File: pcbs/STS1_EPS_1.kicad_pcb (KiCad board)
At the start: 4 copper layers, 81 x 85 mm, 57 parts, among them J2 Panel X+, J3 Battery Pack, J4 Panel X-, J5 Panel Y+, J6 Panel Y-, J7 Panel Z+, Q1 SI7135DP-T1-GE3, U1 LTC4020EUHFPBF, U10 MAX11632EEGT, U4 BQ29209DRBT, U5 MAX11632EEGT, U6 MAX11632EEGT, U7 MAX11632EEGT, U8 MAX11632EEGT, U9 MAX11632EEGT

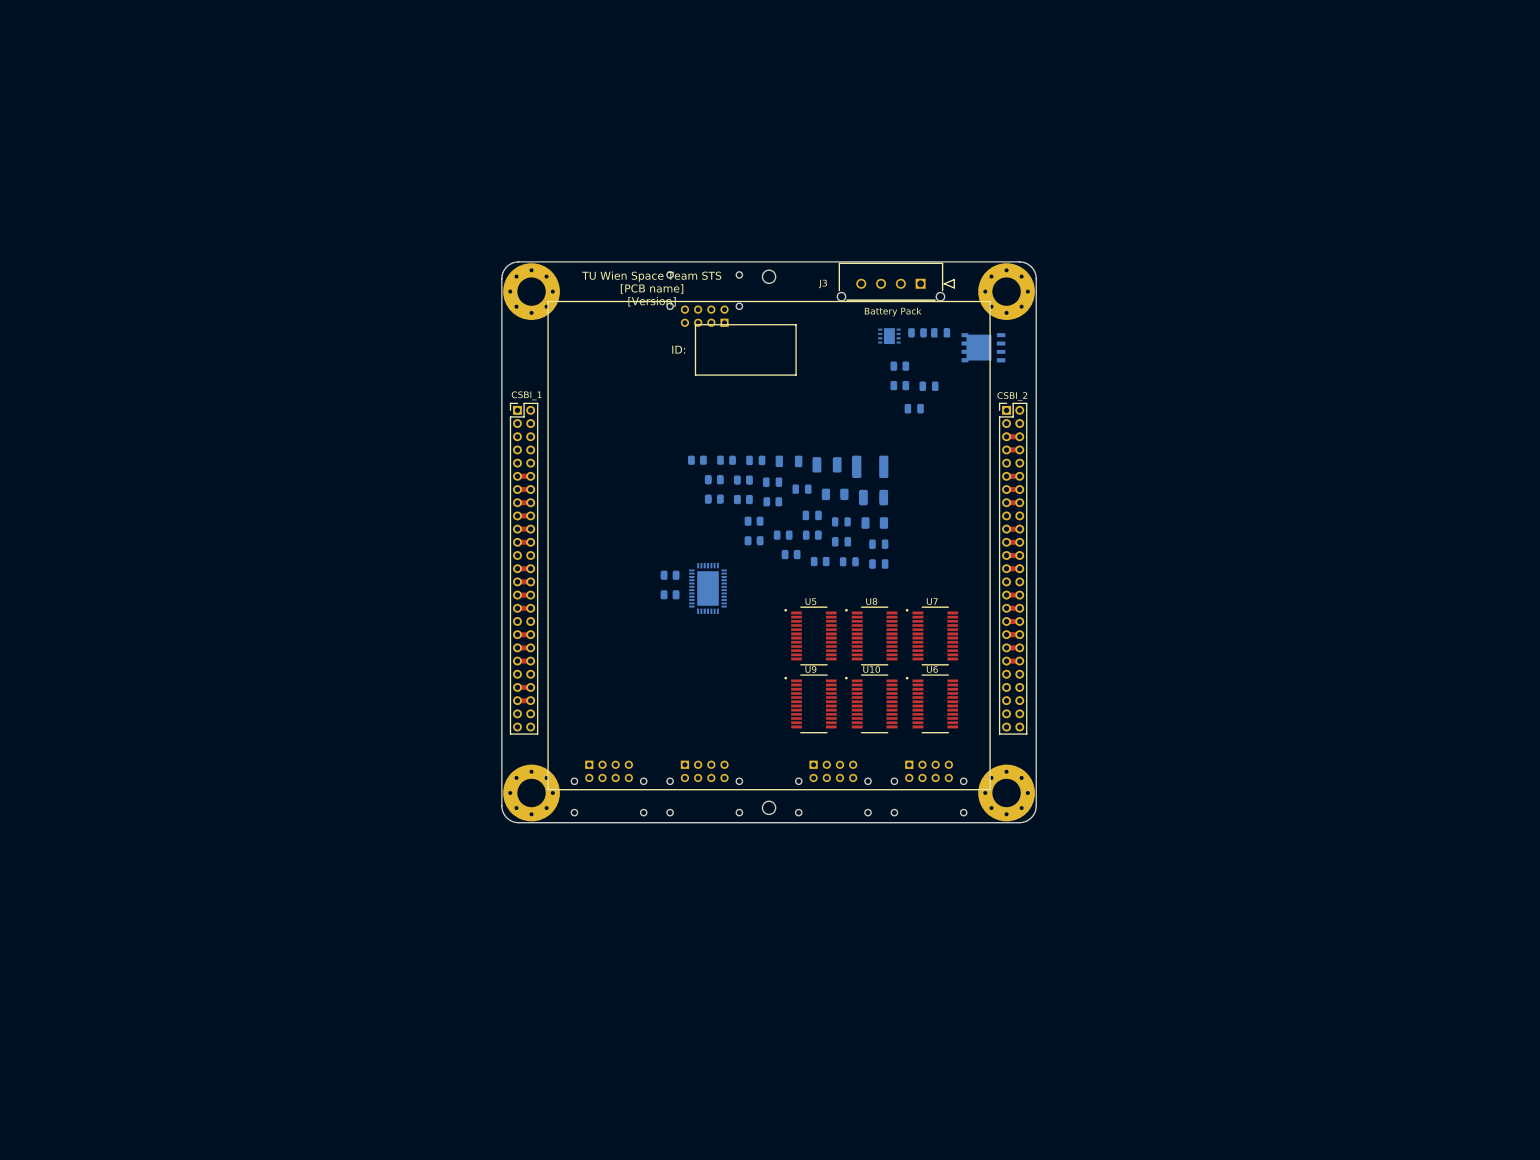
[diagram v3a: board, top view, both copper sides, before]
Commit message: Worked on STS1_EPS_1.
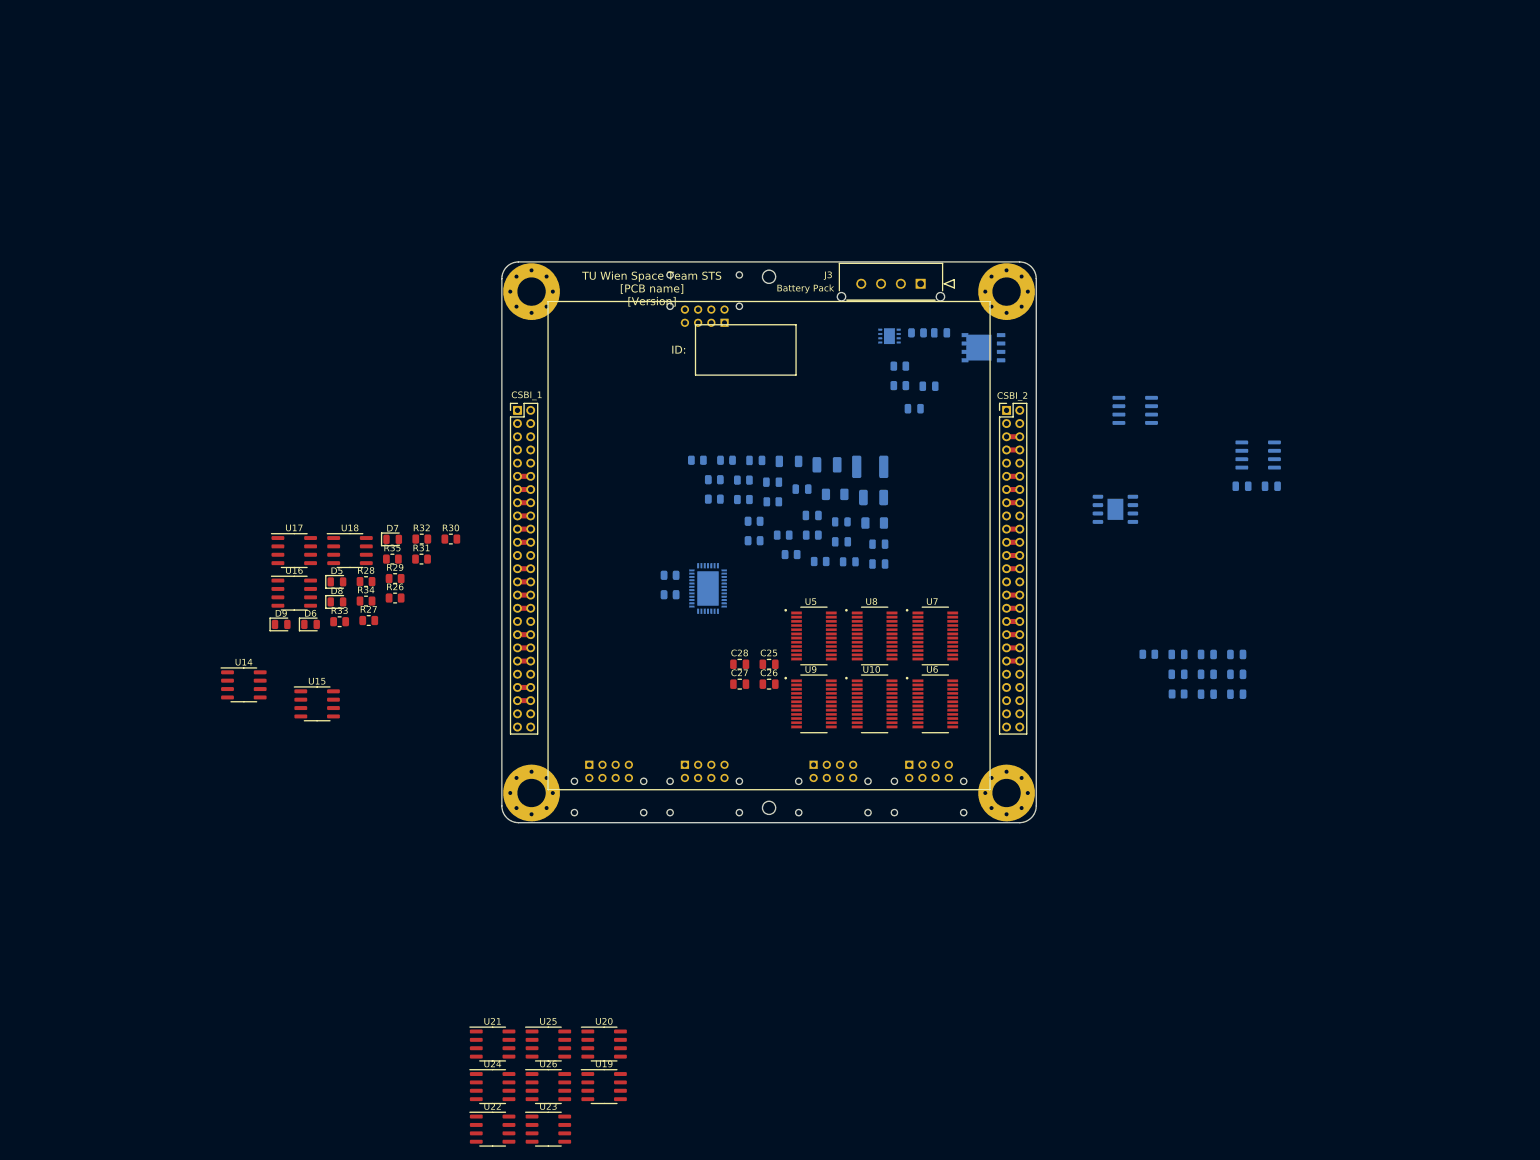
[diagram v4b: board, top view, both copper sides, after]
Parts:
- added C15: 1u, Capacitor_SMD:C_0805_2012Metric, B.Cu at (232.8, 75.8)
- added C16: 1u, Capacitor_SMD:C_0805_2012Metric, B.Cu at (228.3, 75.8)
- added C17: 100n, Capacitor_SMD:C_0805_2012Metric, B.Cu at (218.6, 101.3)
- added C18: 100n, Capacitor_SMD:C_0805_2012Metric, B.Cu at (223.1, 101.3)
- added C19: 100n, Capacitor_SMD:C_0805_2012Metric, B.Cu at (223.1, 104.3)
- added C20: 100n, Capacitor_SMD:C_0805_2012Metric, B.Cu at (227.5, 101.3)
- added C21: 100n, Capacitor_SMD:C_0805_2012Metric, B.Cu at (227.5, 104.3)
- added C22: 100n, Capacitor_SMD:C_0805_2012Metric, B.Cu at (223.1, 107.3)
- added C23: 100n, Capacitor_SMD:C_0805_2012Metric, B.Cu at (218.6, 104.3)
- added C24: 100n, Capacitor_SMD:C_0805_2012Metric, B.Cu at (227.5, 107.3)
- added C25: 100n, Capacitor_SMD:C_0805_2012Metric, F.Cu at (156.6, 102.8)
- added C26: 100n, Capacitor_SMD:C_0805_2012Metric, F.Cu at (156.6, 105.8)
- added C27: 100n, Capacitor_SMD:C_0805_2012Metric, F.Cu at (152.2, 105.8)
- added C28: 100n, Capacitor_SMD:C_0805_2012Metric, F.Cu at (152.2, 102.8)
- added D5: TS4148 RYG, Diode_SMD:D_0805_2012Metric, F.Cu at (91.1, 90.3)
- added D6: TS4148 RYG, Diode_SMD:D_0805_2012Metric, F.Cu at (87.1, 96.8)
- added D7: TS4148 RYG, Diode_SMD:D_0805_2012Metric, F.Cu at (99.6, 83.8)
- added D8: TS4148 RYG, Diode_SMD:D_0805_2012Metric, F.Cu at (91.1, 93.3)
- added D9: TS4148 RYG, Diode_SMD:D_0805_2012Metric, F.Cu at (82.7, 96.8)
- added R24: 87k5, Resistor_SMD:R_0805_2012Metric, B.Cu at (214.2, 101.3)
- added R25: 100k, Resistor_SMD:R_0805_2012Metric, B.Cu at (218.6, 107.3)
- added R26: 332, Resistor_SMD:R_0805_2012Metric, F.Cu at (100.0, 92.7)
- added R27: 3320, Resistor_SMD:R_0805_2012Metric, F.Cu at (96.0, 96.2)
- added R28: 332, Resistor_SMD:R_0805_2012Metric, F.Cu at (95.5, 90.3)
- added R29: 3320, Resistor_SMD:R_0805_2012Metric, F.Cu at (100.0, 89.8)
- added R30: 332, Resistor_SMD:R_0805_2012Metric, F.Cu at (108.4, 83.8)
- added R31: 3320, Resistor_SMD:R_0805_2012Metric, F.Cu at (104.0, 86.8)
- added R32: 332, Resistor_SMD:R_0805_2012Metric, F.Cu at (104.0, 83.8)
- added R33: 3320, Resistor_SMD:R_0805_2012Metric, F.Cu at (91.5, 96.3)
- added R34: 332, Resistor_SMD:R_0805_2012Metric, F.Cu at (95.5, 93.2)
- added R35: 3320, Resistor_SMD:R_0805_2012Metric, F.Cu at (99.5, 86.8)
- added U11: TMCS1101A3B-Q1, Package_SO:SOIC-8_3.9x4.9mm_P1.27mm, B.Cu at (230.8, 71.1)
- added U12: BD50GA5WEFJ, Package_SO:HTSOP-8-1EP_3.9x4.9mm_P1.27mm_EP2.4x3.2mm, B.Cu at (209.1, 79.3)
- added U13: TMCS1101A3B-Q1, Package_SO:SOIC-8_3.9x4.9mm_P1.27mm, B.Cu at (212.1, 64.3)
- added U14: LM334M, Package_SO:SOIC-8_3.9x4.9mm_P1.27mm, F.Cu at (77.0, 105.9)
- added U15: LM334M, Package_SO:SOIC-8_3.9x4.9mm_P1.27mm, F.Cu at (88.1, 108.8)
- added U16: LM334M, Package_SO:SOIC-8_3.9x4.9mm_P1.27mm, F.Cu at (84.7, 92.0)
- added U17: LM334M, Package_SO:SOIC-8_3.9x4.9mm_P1.27mm, F.Cu at (84.7, 85.6)
- added U18: LM334M, Package_SO:SOIC-8_3.9x4.9mm_P1.27mm, F.Cu at (93.1, 85.6)
- added U19: TMCS1101A3B-Q1, Package_SO:SOIC-8_3.9x4.9mm_P1.27mm, F.Cu at (131.6, 166.8)
- added U20: TMCS1101A3B-Q1, Package_SO:SOIC-8_3.9x4.9mm_P1.27mm, F.Cu at (131.6, 160.3)
- added U21: TMCS1101A3B-Q1, Package_SO:SOIC-8_3.9x4.9mm_P1.27mm, F.Cu at (114.7, 160.3)
- added U22: TMCS1101A3B-Q1, Package_SO:SOIC-8_3.9x4.9mm_P1.27mm, F.Cu at (114.7, 173.2)
- added U23: TMCS1101A3B-Q1, Package_SO:SOIC-8_3.9x4.9mm_P1.27mm, F.Cu at (123.2, 173.2)
- added U24: TMCS1101A3B-Q1, Package_SO:SOIC-8_3.9x4.9mm_P1.27mm, F.Cu at (114.7, 166.8)
- added U25: TMCS1101A3B-Q1, Package_SO:SOIC-8_3.9x4.9mm_P1.27mm, F.Cu at (123.2, 160.3)
- added U26: TMCS1101A3B-Q1, Package_SO:SOIC-8_3.9x4.9mm_P1.27mm, F.Cu at (123.2, 166.8)
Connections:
- net /Analog Digital Converters/VOUT renamed /Battery Charge Controller/VOUT
- net /Battery/BAT_FAULT renamed /BAT_FAULT
- J3 pad 1: /Battery Charge Controller/BATT -> /BATT_RAW
- J3 pad 3: /Battery/NTC -> /NTC
- J3 pad 4: /Battery/CENTER -> /CENTER
- R21 pad 2: /Battery/CENTER -> /CENTER
- R23 pad 1: /Battery/CENTER -> /CENTER
- U1 pad 16: /Battery/NTC -> /NTC
- U1 pad 36: /Panel_X+_3 -> /MPPT_BUS
- U10 pad 1: unconnected-(U10-Pad1) -> /Panel_X+_1
- U10 pad 10: unconnected-(U10-Pad10) -> /Panel_X+_7
- U10 pad 11: unconnected-(U10-Pad11) -> /Panel_X-_2
- U10 pad 12: unconnected-(U10-Pad12) -> /Panel_X-_7
- U10 pad 13: unconnected-(U10-Pad13) -> /Panel_Y+_2
- U10 pad 14: unconnected-(U10-Pad14) -> /Panel_Y-_2
- U10 pad 15: unconnected-(U10-Pad15) -> /Panel_Z+_2
- U10 pad 16: unconnected-(U10-Pad16) -> /Panel_Z+_7
- U10 pad 17: unconnected-(U10-Pad17) -> /Analog Digital Converters/REF4
- U10 pad 19: unconnected-(U10-Pad19) -> /5V
- U10 pad 2: unconnected-(U10-Pad2) -> /Panel_X+_8
- U10 pad 20: unconnected-(U10-Pad20) -> /Analog Digital Converters/COBC_SPI_4
- U10 pad 21: unconnected-(U10-Pad21) -> /Analog Digital Converters/COBC_SPI_1
- U10 pad 22: unconnected-(U10-Pad22) -> /Analog Digital Converters/COBC_SPI_2
- U10 pad 23: unconnected-(U10-Pad23) -> /Analog Digital Converters/COBC_SPI_3
- U10 pad 3: unconnected-(U10-Pad3) -> /Panel_X-_1
- U10 pad 4: unconnected-(U10-Pad4) -> /Panel_X-_8
- U10 pad 5: unconnected-(U10-Pad5) -> /Panel_Y+_1
- U10 pad 6: unconnected-(U10-Pad6) -> /Panel_Y-_1
- U10 pad 7: unconnected-(U10-Pad7) -> /Panel_Z+_1
- U10 pad 8: unconnected-(U10-Pad8) -> /Panel_Z+_8
- U10 pad 9: unconnected-(U10-Pad9) -> /Panel_X+_2
- U4 pad 7: /Battery Charge Controller/BATT -> /BATT_RAW
- U5 pad 1: unconnected-(U5-Pad1) -> /Panel_X+_1
- U5 pad 10: unconnected-(U5-Pad10) -> /Panel_X+_7
- U5 pad 11: unconnected-(U5-Pad11) -> /Panel_X-_2
- U5 pad 12: unconnected-(U5-Pad12) -> /Panel_X-_7
- U5 pad 13: unconnected-(U5-Pad13) -> /Panel_Y+_2
- U5 pad 14: unconnected-(U5-Pad14) -> /Panel_Y-_2
- U5 pad 15: unconnected-(U5-Pad15) -> /Panel_Z+_2
- U5 pad 16: unconnected-(U5-Pad16) -> /Panel_Z+_7
- U5 pad 17: unconnected-(U5-Pad17) -> /Analog Digital Converters/REF1
- U5 pad 19: unconnected-(U5-Pad19) -> /5V
- U5 pad 2: unconnected-(U5-Pad2) -> /Panel_X+_8
- U5 pad 20: unconnected-(U5-Pad20) -> /Analog Digital Converters/EDU_SPI_4
- U5 pad 21: unconnected-(U5-Pad21) -> /Analog Digital Converters/EDU_SPI_1
- U5 pad 22: /Analog Digital Converters/Panel_X+_2 -> /Analog Digital Converters/EDU_SPI_2
- U5 pad 23: unconnected-(U5-Pad23) -> /Analog Digital Converters/EDU_SPI_3
- U5 pad 3: unconnected-(U5-Pad3) -> /Panel_X-_1
- U5 pad 4: unconnected-(U5-Pad4) -> /Panel_X-_8
- U5 pad 5: unconnected-(U5-Pad5) -> /Panel_Y+_1
- U5 pad 6: unconnected-(U5-Pad6) -> /Panel_Y-_1
- U5 pad 7: unconnected-(U5-Pad7) -> /Panel_Z+_1
- U5 pad 8: unconnected-(U5-Pad8) -> /Panel_Z+_8
- U5 pad 9: unconnected-(U5-Pad9) -> /Panel_X+_2
- U6 pad 1: unconnected-(U6-Pad1) -> /Analog Digital Converters/BATT_SCALED
- U6 pad 10: unconnected-(U6-Pad10) -> GND
- U6 pad 11: unconnected-(U6-Pad11) -> GND
- U6 pad 12: unconnected-(U6-Pad12) -> GND
- U6 pad 13: unconnected-(U6-Pad13) -> GND
- U6 pad 14: unconnected-(U6-Pad14) -> GND
- U6 pad 15: unconnected-(U6-Pad15) -> GND
- U6 pad 16: unconnected-(U6-Pad16) -> GND
- U6 pad 17: unconnected-(U6-Pad17) -> /Analog Digital Converters/REF5
- U6 pad 19: unconnected-(U6-Pad19) -> /5V
- U6 pad 2: unconnected-(U6-Pad2) -> /CENTER
- U6 pad 20: unconnected-(U6-Pad20) -> /Analog Digital Converters/COBC_SPI_5
- U6 pad 21: unconnected-(U6-Pad21) -> /Analog Digital Converters/COBC_SPI_1
- U6 pad 22: unconnected-(U6-Pad22) -> /Analog Digital Converters/COBC_SPI_2
- U6 pad 23: unconnected-(U6-Pad23) -> /Analog Digital Converters/COBC_SPI_3
- U6 pad 3: unconnected-(U6-Pad3) -> /BATT_I
- U6 pad 4: unconnected-(U6-Pad4) -> /NTC
- U6 pad 5: unconnected-(U6-Pad5) -> /Panel_X+_5
- U6 pad 6: unconnected-(U6-Pad6) -> /Panel_X-_5
- U6 pad 7: unconnected-(U6-Pad7) -> /Panel_Y+_5
- U6 pad 8: unconnected-(U6-Pad8) -> /Panel_Y-_5
- U6 pad 9: unconnected-(U6-Pad9) -> /Panel_Z+_5
- U7 pad 1: unconnected-(U7-Pad1) -> /Analog Digital Converters/MPPT_I_SUM
- U7 pad 10: unconnected-(U7-Pad10) -> /MPPT_BUS
- U7 pad 17: unconnected-(U7-Pad17) -> /Analog Digital Converters/REF6
- U7 pad 19: unconnected-(U7-Pad19) -> /5V
- U7 pad 2: unconnected-(U7-Pad2) -> /Analog Digital Converters/MPPT_I_X+_1
- U7 pad 20: unconnected-(U7-Pad20) -> /Analog Digital Converters/COBC_SPI_6
- U7 pad 21: unconnected-(U7-Pad21) -> /Analog Digital Converters/COBC_SPI_1
- U7 pad 22: unconnected-(U7-Pad22) -> /Analog Digital Converters/COBC_SPI_2
- U7 pad 23: unconnected-(U7-Pad23) -> /Analog Digital Converters/COBC_SPI_3
- U7 pad 3: unconnected-(U7-Pad3) -> /Analog Digital Converters/MPPT_I_X+_2
- U7 pad 4: unconnected-(U7-Pad4) -> /Analog Digital Converters/MPPT_I_X-_1
- U7 pad 5: unconnected-(U7-Pad5) -> /Analog Digital Converters/MPPT_I_X-_2
- U7 pad 6: unconnected-(U7-Pad6) -> /Analog Digital Converters/MPPT_I_Y+_1
- U7 pad 7: unconnected-(U7-Pad7) -> /Analog Digital Converters/MPPT_I_Y-_1
- U7 pad 8: unconnected-(U7-Pad8) -> /MPPT_I_Z+_1
- U7 pad 9: unconnected-(U7-Pad9) -> /Analog Digital Converters/MPPT_I_Z+_2
- U8 pad 1: unconnected-(U8-Pad1) -> /Analog Digital Converters/BATT_SCALED
- U8 pad 10: unconnected-(U8-Pad10) -> GND
- U8 pad 11: unconnected-(U8-Pad11) -> GND
- U8 pad 12: unconnected-(U8-Pad12) -> GND
- U8 pad 13: unconnected-(U8-Pad13) -> GND
- U8 pad 14: unconnected-(U8-Pad14) -> GND
- U8 pad 15: unconnected-(U8-Pad15) -> GND
- U8 pad 16: unconnected-(U8-Pad16) -> GND
- U8 pad 17: unconnected-(U8-Pad17) -> /Analog Digital Converters/REF2
- U8 pad 19: unconnected-(U8-Pad19) -> /5V
- U8 pad 2: unconnected-(U8-Pad2) -> /CENTER
- U8 pad 20: unconnected-(U8-Pad20) -> /Analog Digital Converters/EDU_SPI_5
- U8 pad 21: unconnected-(U8-Pad21) -> /Analog Digital Converters/EDU_SPI_1
- U8 pad 22: unconnected-(U8-Pad22) -> /Analog Digital Converters/EDU_SPI_2
- U8 pad 23: unconnected-(U8-Pad23) -> /Analog Digital Converters/EDU_SPI_3
- U8 pad 3: unconnected-(U8-Pad3) -> /BATT_I
- U8 pad 4: unconnected-(U8-Pad4) -> /NTC
- U8 pad 5: unconnected-(U8-Pad5) -> /Panel_X+_5
- U8 pad 6: unconnected-(U8-Pad6) -> /Panel_X-_5
- U8 pad 7: unconnected-(U8-Pad7) -> /Panel_Y+_5
- U8 pad 8: unconnected-(U8-Pad8) -> /Panel_Y-_5
- U8 pad 9: unconnected-(U8-Pad9) -> /Panel_Z+_5
- U9 pad 1: unconnected-(U9-Pad1) -> /Analog Digital Converters/MPPT_I_SUM
- U9 pad 10: unconnected-(U9-Pad10) -> /MPPT_BUS
- U9 pad 17: unconnected-(U9-Pad17) -> /Analog Digital Converters/REF3
- U9 pad 19: unconnected-(U9-Pad19) -> /5V
- U9 pad 2: unconnected-(U9-Pad2) -> /Analog Digital Converters/MPPT_I_X+_1
- U9 pad 20: unconnected-(U9-Pad20) -> /Analog Digital Converters/EDU_SPI_6
- U9 pad 21: unconnected-(U9-Pad21) -> /Analog Digital Converters/EDU_SPI_1
- U9 pad 22: unconnected-(U9-Pad22) -> /Analog Digital Converters/EDU_SPI_2
- U9 pad 23: unconnected-(U9-Pad23) -> /Analog Digital Converters/EDU_SPI_3
- U9 pad 3: unconnected-(U9-Pad3) -> /Analog Digital Converters/MPPT_I_X+_2
- U9 pad 4: unconnected-(U9-Pad4) -> /Analog Digital Converters/MPPT_I_X-_1
- U9 pad 5: unconnected-(U9-Pad5) -> /Analog Digital Converters/MPPT_I_X-_2
- U9 pad 6: unconnected-(U9-Pad6) -> /Analog Digital Converters/MPPT_I_Y+_1
- U9 pad 7: unconnected-(U9-Pad7) -> /Analog Digital Converters/MPPT_I_Y-_1
- U9 pad 8: unconnected-(U9-Pad8) -> /MPPT_I_Z+_1
- U9 pad 9: unconnected-(U9-Pad9) -> /Analog Digital Converters/MPPT_I_Z+_2
